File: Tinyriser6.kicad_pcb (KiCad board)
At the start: 2 copper layers, 113.2 x 55.1 mm, 60 parts, among them J1 Bus_M.2_Socket_M, J2 Bus_PCI_Express_x16, J3 Bus_M.2_Socket_M, J3 Conn_02x04_Odd_Even, J5 Conn_02x04_Odd_Even, M1 Fan_4pin

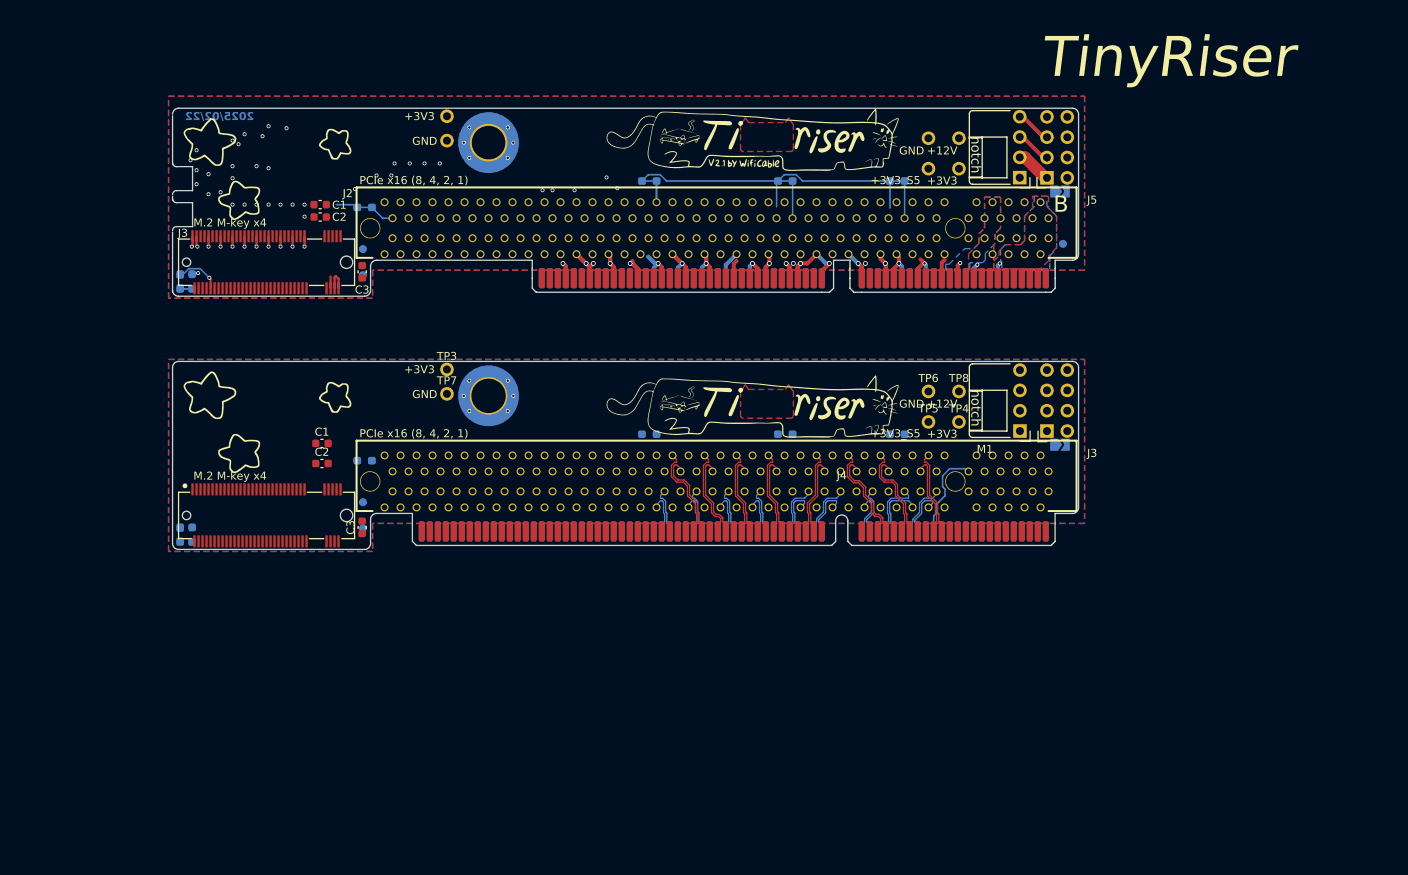
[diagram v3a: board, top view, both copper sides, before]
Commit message: Added random io header, usb and started routing M.2 PCIe
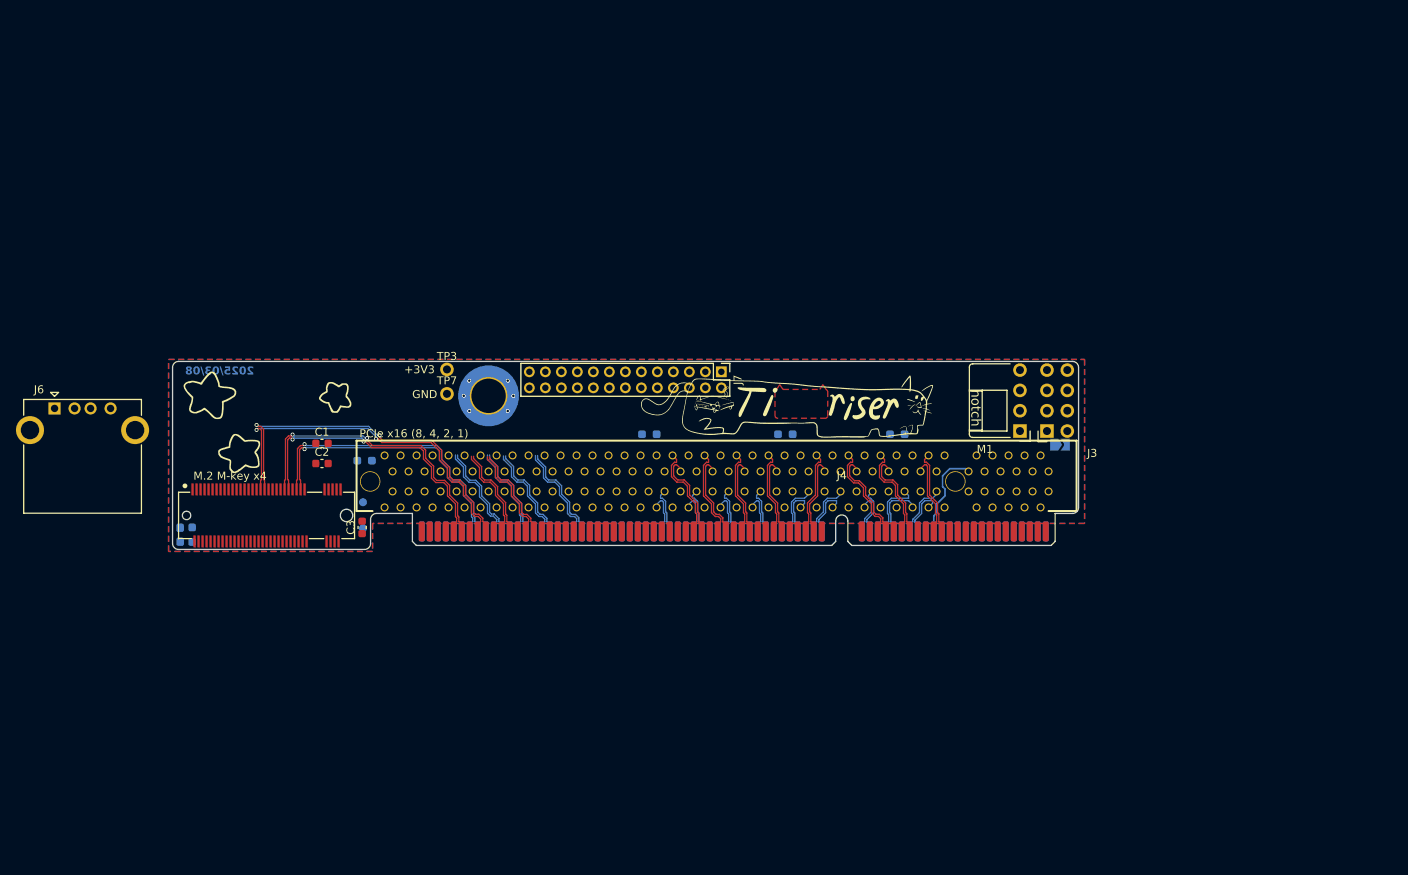
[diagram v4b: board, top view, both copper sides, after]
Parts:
- removed the C1 at (139.7, 43.1)
- removed the C2 at (139.7, 44.7)
- removed the C3 at (144.9, 51.5)
- removed the D1 at (122.2, 52.8)
- removed the G*** at (222.3, 37.0)
- removed the G*** at (132.7, 41.1)
- removed the G*** at (193.8, 34.6) (x2)
- removed the G*** at (133.7, 38.6)
- removed the G*** at (192.6, 37.9)
- removed the H1 at (160.8, 35.4)
- removed the J1 at (205.2, 48.6)
- removed the J2 at (189.2, 46.1)
- removed the J3 at (133.0, 50.4)
- removed J5: Conn_02x04_Odd_Even, Connector_PinSocket_2.54mm:PinSocket_2x04_P2.54mm_Horizontal
- removed the JP1 at (232.2, 41.5)
- removed the M1 at (227.2, 39.8)
- removed the R1 at (123.7, 52.8)
- removed the R3 at (145.2, 43.5)
- removed the R4 at (180.8, 40.2)
- removed the R5 at (197.8, 40.2)
- removed R6: 0R, Resistor_SMD:R_0603_1608Metric_Pad0.98x0.95mm_HandSolder
- removed the TP1 at (232.6, 48.0)
- removed the TP2 at (145.1, 52.0)
- removed the TP3 at (145.1, 48.7)
- removed TP4 (x2), TP8: +3V3, TestPoint:TestPoint_THTPad_D1.5mm_Drill0.7mm
- removed TP5 (x2): +3V3_S5, TestPoint:TestPoint_THTPad_D1.5mm_Drill0.7mm
- removed TP6 (x2): GND, TestPoint:TestPoint_THTPad_D1.5mm_Drill0.7mm
- removed the TP7 at (155.6, 35.1)
- removed TP8, TP9: +12V, TestPoint:TestPoint_THTPad_D1.5mm_Drill0.7mm
- added J6: USB_A, Connector_USB:USB_A_CONNFLY_DS1095-WNR0, F.Cu at (106.5, 68.6)
- added J7: Conn_01x26_Pin, Connector_PinHeader_2.00mm:PinHeader_2x13_P2.00mm_Vertical, F.Cu at (189.8, 64.0)
- moved G*** 4.30 mm to (198.1, 68.0) (x2)
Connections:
- J4 pad A1: unconnected-(J4-PCIe_CPU_REFCLK1--PadA1) -> PCIe_CPU_REFCLK1-
- J4 pad A17: unconnected-(J4-PCIe_CPU_REFCLK5+-PadA17) -> PCIe_CPU_REFCLK5+
- J4 pad A18: unconnected-(J4-PCIe_CPU_REFCLK5--PadA18) -> PCIe_CPU_REFCLK5-
- J4 pad A19: Net-(J4-GPU_PWR_EN) -> GPU_PWR_EN
- J4 pad A2: unconnected-(J4-PCIe_CPU_REFCLK1+-PadA2) -> PCIe_CPU_REFCLK1+
- J4 pad A20: Net-(J4-GPU_MACO_EN) -> GPU_MACO_EN
- J4 pad A21: unconnected-(J4-AZ_SDOUT_R(ME_DISABLE)-PadA21) -> AZ_SDOUT_R
- J4 pad A22: unconnected-(J4-ESPI_ALERT0#_BMC@-PadA22) -> ESPI_ALERT0#_BMC
- J4 pad A23: unconnected-(J4-ESPI_ALERT1#@-PadA23) -> ESPI_ALERT1#
- J4 pad A24: unconnected-(J4-SIO_SML1ALERT#-PadA24) -> SIO_SML1ALERT#
- J4 pad A25: unconnected-(J4-ESPI_IO1_BMC@-PadA25) -> ESPI_IO1_BMC
- J4 pad A26: unconnected-(J4-ESPI_RESET#_BMC@-PadA26) -> ESPI_RESET#_BMC
- J4 pad A27: unconnected-(J4-ME_RECOVERY_BMC-PadA27) -> ME_RECOVERY_BMC
- J4 pad A28: unconnected-(J4-SMLINK1_DATA-PadA28) -> SMLINK1_DATA
- J4 pad A29: unconnected-(J4-SMLINK1_CLK-PadA29) -> SMLINK1_CLK
- J4 pad A3: unconnected-(J4-PCH_SYSPOWEROK-PadA3) -> PCH_SYSPOWEROK
- J4 pad A30: unconnected-(J4-PCIE_X8_X4_PRSNT#-PadA30) -> PCIE_X8_X4_PRSNT#
- J4 pad A31: unconnected-(J4-ESPI_IO0_BMC@-PadA31) -> ESPI_IO0_BMC
- J4 pad A32: unconnected-(J4-ESPI_CLK_BMC@-PadA32) -> ESPI_CLK_BMC
- J4 pad A4: unconnected-(J4-BMC_DETECT#(CLKREQ1,5,11,CFG6)@-PadA4) -> BMC_DETECT#
- J4 pad B1: unconnected-(J4-@ESPI_CS1#_BMC-PadB1) -> ESPI_CS1#_BMC
- J4 pad B2: unconnected-(J4-@ESPI_CS0#_BMC-PadB2) -> ESPI_CS0#_BMC
- J4 pad B23: unconnected-(J4-PCIe_CPU_REFCLK11--PadB23) -> PCIe_CPU_REFCLK11-
- J4 pad B24: unconnected-(J4-PCIe_CPU_REFCLK11+-PadB24) -> PCIe_CPU_REFCLK11+
- J4 pad B25: unconnected-(J4-PWRBTN#-PadB25) -> PWRBTN#
- J4 pad B26: unconnected-(J4-USB_D--PadB26) -> USB_D-
- J4 pad B27: unconnected-(J4-USB_D+-PadB27) -> USB_D+
- J4 pad B28: unconnected-(J4-FP_RST#-PadB28) -> FP_RST#
- J4 pad B3: unconnected-(J4-+5V_S5-PadB3) -> +5V
- J4 pad B4: unconnected-(J4-+5V_S5-PadB4) -> +5V
- J4 pad B5: unconnected-(J4-+5V_S5-PadB5) -> +5V
- J4 pad B6: unconnected-(J4-RSMRST_SIO#-PadB6) -> RSMRST_SIO#
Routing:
- net GND: track 121.1 -> 0.00 mm, vias 82 -> 6
- net PCIe_CPU_CLKREQ#: track 64.2 -> 0.00 mm
- net PCIe_PCH_Tx1+: track 0.00 -> 46.4 mm, vias 0 -> 2
- net PCIe_PCH_Tx1-: track 0.00 -> 45.6 mm, vias 0 -> 2
- net PCIe_PCH_Tx0-: track 0.00 -> 37.7 mm, vias 0 -> 2
- net PCIe_PCH_Tx0+: track 0.00 -> 36.8 mm, vias 0 -> 2
- net PCIe_PCH_REFCLK-: track 0.00 -> 36.3 mm, vias 0 -> 1
- net PCIe_PCH_REFCLK+: track 0.00 -> 35.4 mm, vias 0 -> 1
- net PCIe_PCH_Rx3-: track 0.00 -> 12.6 mm
- net PCIe_PCH_Rx3+: track 0.00 -> 12.6 mm
- net PCIe_PCH_Rx0+: track 0.00 -> 12.4 mm
- net PCIe_PCH_Rx0-: track 0.00 -> 12.4 mm
- net PCIe_PCH_Rx2+: track 0.00 -> 12.4 mm
- net PCIe_PCH_Rx2-: track 0.00 -> 12.4 mm
- net PCIe_PCH_Tx3+: track 0.00 -> 12.4 mm
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- removed copper zone on B.Cu, net +12V
- removed copper zone on F.Cu, net +12V
- removed copper zone on B.Cu, net +3V3
- removed copper zone on F.Cu, net +3V3
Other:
- board size 113.2 x 55.1 mm -> 113.2 x 23.5 mm
- board text added: "2025/03/08"
- board text removed: "+12V"
- board text removed: "+3V3_S5"
- board text removed: "2025/02/22"
- board text removed: "Compatible with Tiny5: Lenovo ThinkCentre M720q, M920q, M920x Tiny Lenovo ThinkStation P330 Tiny NEC Mate MC-3, MC-4, MC-5"
- board text removed: "PCIE_SOLT_A60"
- board text removed: "TinyRiser"

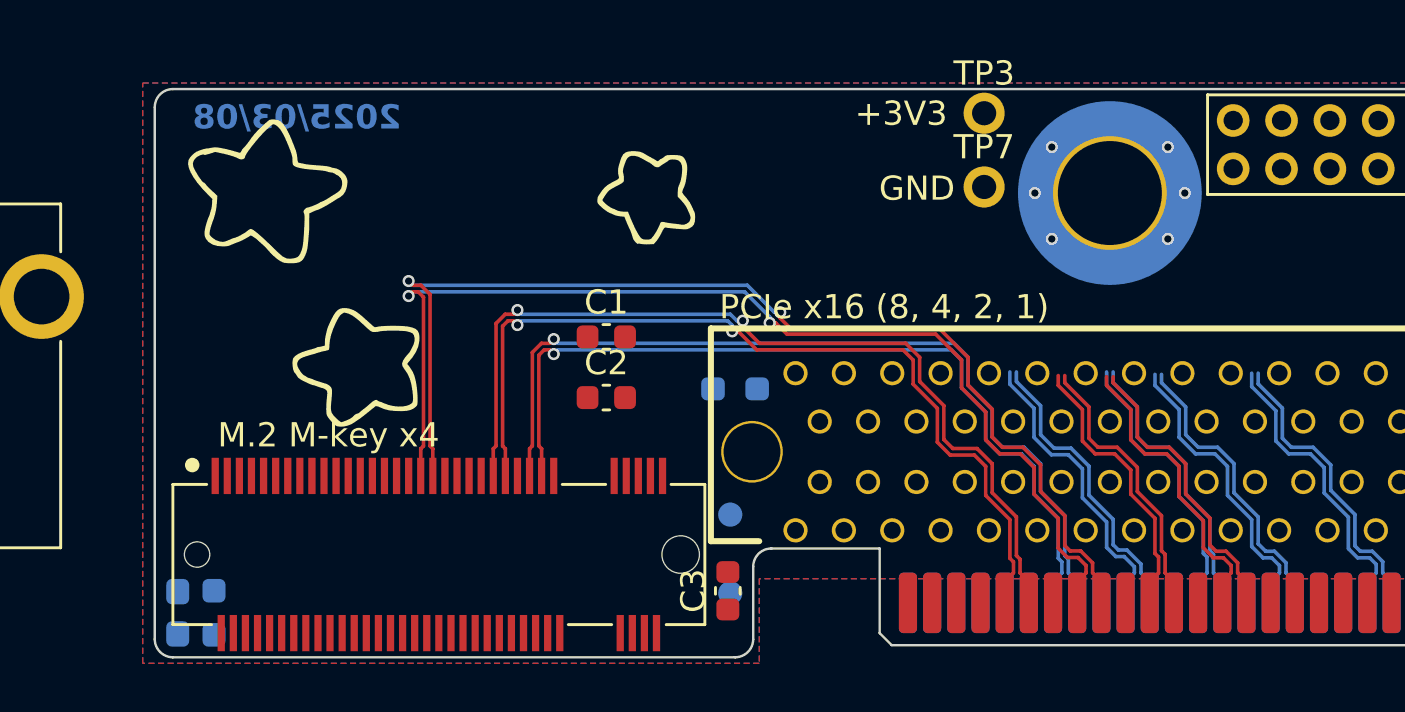
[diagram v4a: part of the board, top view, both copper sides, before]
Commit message: Finished routing M.2 PCIe lanes
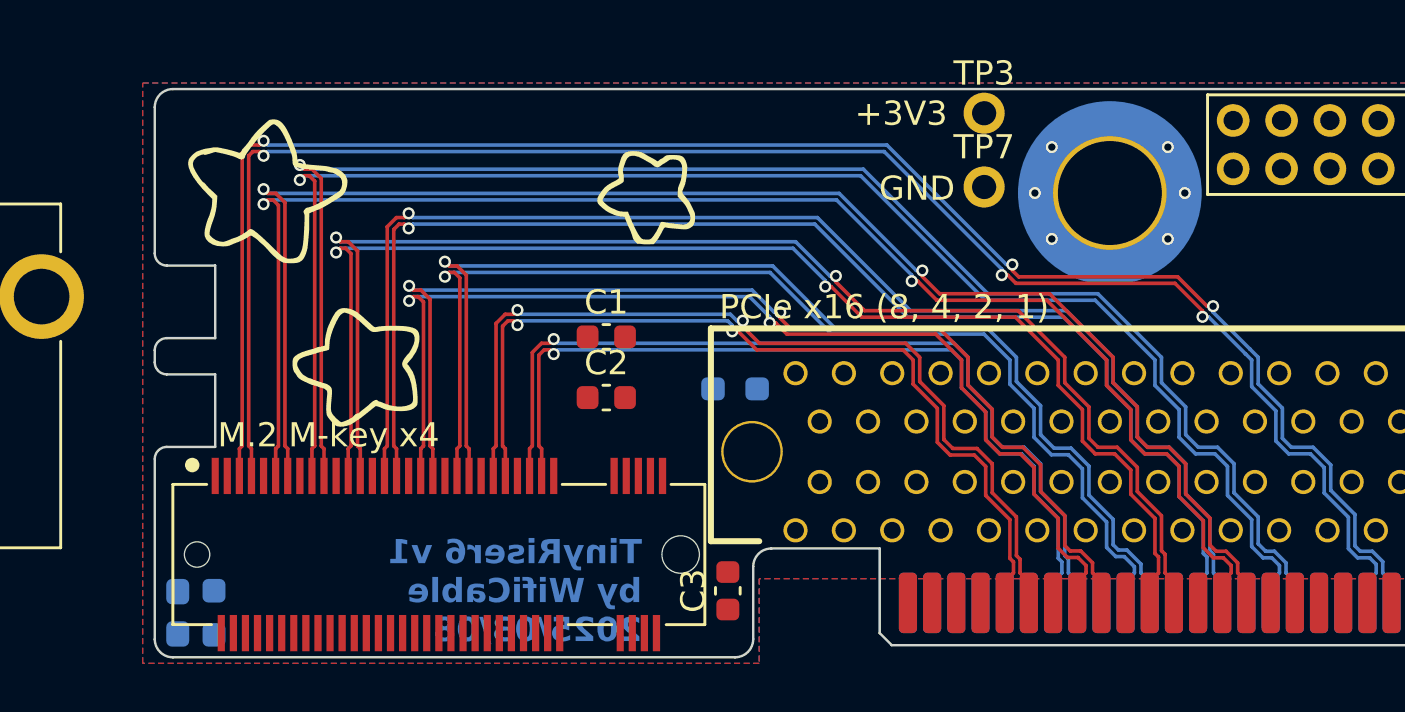
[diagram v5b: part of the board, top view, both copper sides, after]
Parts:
- removed TP1: GPU_PWR_EN, TestPoint:TestPoint_Pad_D1.0mm
- removed TP2: GPU_MACO_EN, TestPoint:TestPoint_Pad_D1.0mm
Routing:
- net PCIe_PCH_Rx3-: track 12.6 -> 72.9 mm, vias 0 -> 3
- net PCIe_PCH_Rx3+: track 12.6 -> 72.0 mm, vias 0 -> 3
- net PCIe_PCH_Rx2+: track 12.4 -> 65.5 mm, vias 0 -> 1
- net PCIe_PCH_Rx2-: track 12.4 -> 64.6 mm, vias 0 -> 1
- net PCIe_PCH_Tx3+: track 12.4 -> 63.8 mm, vias 0 -> 2
- net PCIe_PCH_Tx3-: track 12.4 -> 62.9 mm, vias 0 -> 2
- net PCIe_PCH_Rx1-: track 11.9 -> 55.6 mm, vias 0 -> 1
- net PCIe_PCH_Tx2+: track 11.7 -> 55.3 mm, vias 0 -> 2
- net PCIe_PCH_Rx1+: track 11.9 -> 54.7 mm, vias 0 -> 1
- net PCIe_PCH_Tx2-: track 11.7 -> 54.4 mm, vias 0 -> 2
- net PCIe_PCH_Rx0+: track 12.4 -> 47.8 mm, vias 0 -> 1
- net PCIe_PCH_Rx0-: track 12.4 -> 46.9 mm, vias 0 -> 1
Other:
- outline, holes or cut-outs redrawn
- board text added: "TinyRiser6 v1 by WifiCable 2025/03/08"
- board text removed: "2025/03/08"
- board text removed: "GPU_MACO_EN"
- board text removed: "GPU_PWR_EN"

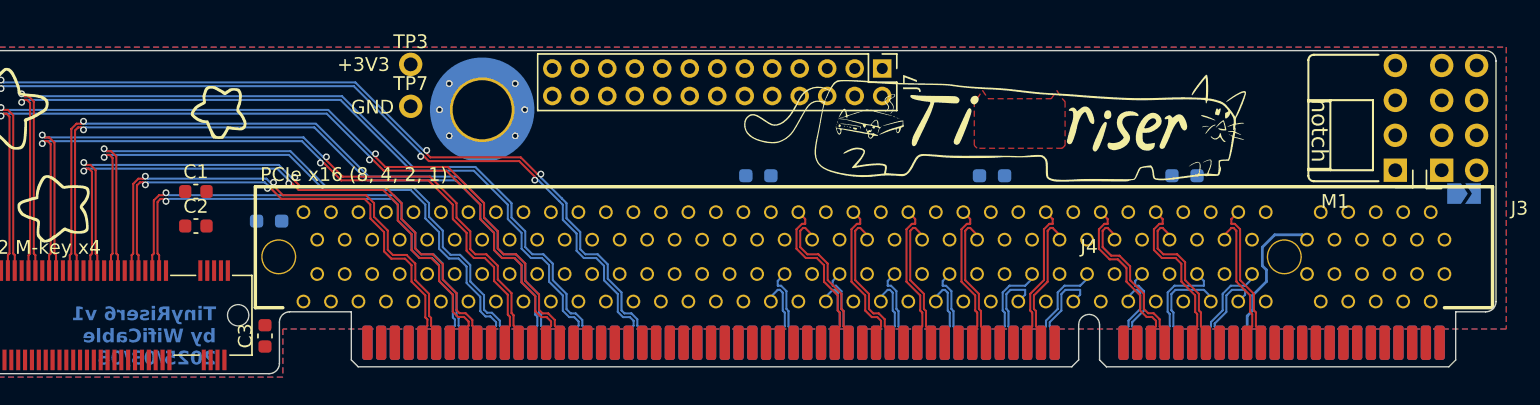
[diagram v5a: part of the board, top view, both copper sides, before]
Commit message: routed power and some misc signals
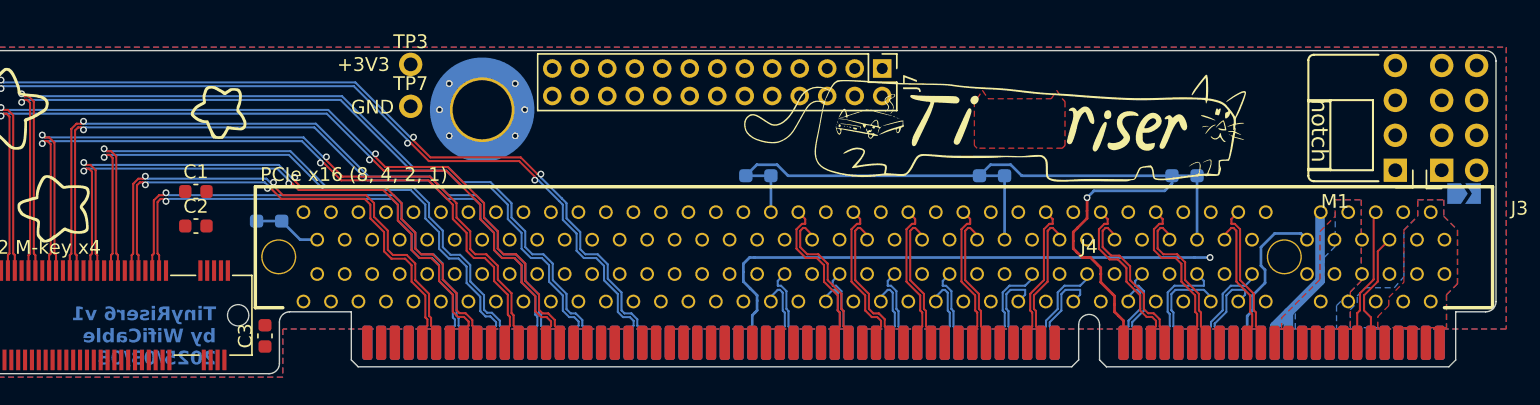
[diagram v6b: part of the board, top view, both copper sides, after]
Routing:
- net PCIe_CPU_CLKREQ#: track 0.00 -> 62.8 mm, vias 0 -> 1
- net PERST#: track 0.00 -> 48.4 mm, vias 0 -> 1
- net +3V3_S5: track 0.00 -> 13.1 mm
- net SMBDATA: track 0.00 -> 10.1 mm
- net SMBCLK: track 0.00 -> 8.47 mm
- net Net-(J2-~{PRSNT2}-PadB31): track 0.00 -> 4.65 mm
- net Net-(J2-~{PRSNT2}-PadB17): track 0.00 -> 4.65 mm
- net Net-(J2-~{PRSNT2}-PadB48): track 0.00 -> 2.65 mm
- added copper zone on B.Cu, net +12V
- added copper zone on F.Cu, net +12V
- added copper zone on B.Cu, net +3V3
- added copper zone on F.Cu, net +3V3
- added copper zone on In1.Cu, net GND
- added copper zone on In2.Cu, net GND
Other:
- copper layers 2 -> 4

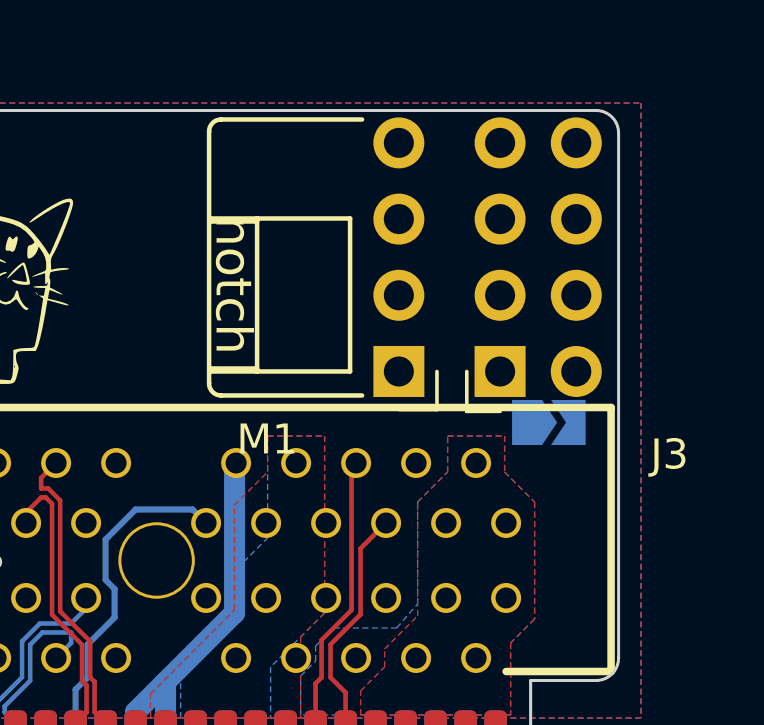
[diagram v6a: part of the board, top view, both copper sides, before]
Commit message: wired up fan header
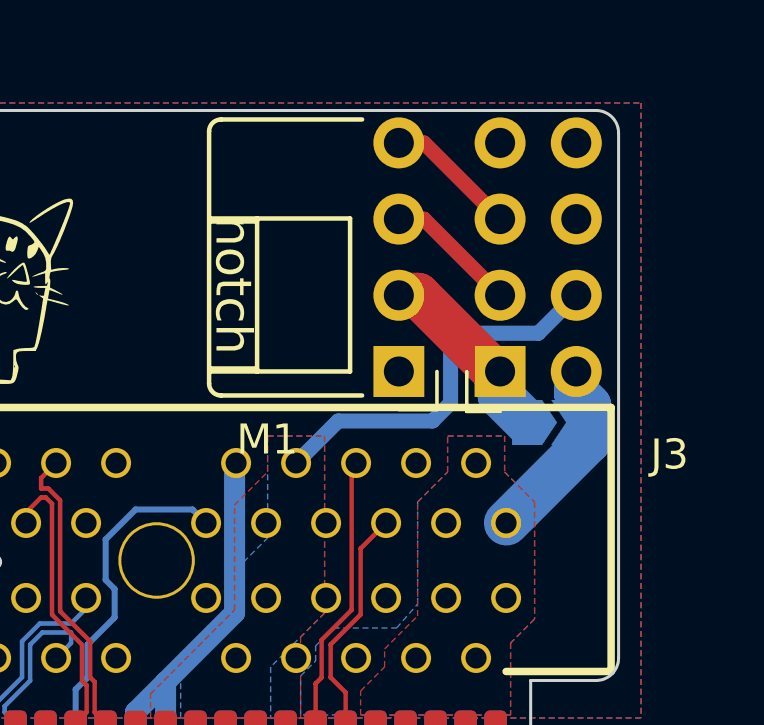
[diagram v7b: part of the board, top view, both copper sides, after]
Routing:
- net SMBCLK: track 8.47 -> 25.9 mm
- net SMBDATA: track 10.1 -> 24.4 mm
- net +3V3: track 0.00 -> 12.8 mm
- net +12V_fan: track 0.00 -> 6.50 mm
- net +12V: track 0.00 -> 6.36 mm
- net Taco_fan: track 0.00 -> 4.43 mm
- net PWM_fan: track 0.00 -> 4.43 mm
